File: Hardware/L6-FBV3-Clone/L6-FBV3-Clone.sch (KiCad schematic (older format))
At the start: 25 parts, among them J1 Conn_02x20_Odd_Even, SW1 SW_Push, SW10 SW_Push, SW11 SW_Push, SW12 SW_Push, SW2 SW_Push, SW3 SW_Push, SW4 SW_Push, SW5 SW_Push, SW6 SW_Push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

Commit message: Fixed schematic rule check, assigned components
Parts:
- added J2: PWR, TerminalBlock_Phoenix:TerminalBlock_Phoenix_MPT-0,5-2-2.54_1x02_P2.54mm_Horizontal, symbol Connector:Screw_Terminal_01x02
- D1, D10, D2, D3, D4, D5, D6, D7, D8, D9: footprint (none) -> TerminalBlock_Phoenix:TerminalBlock_Phoenix_MPT-0,5-2-2.54_1x02_P2.54mm_Horizontal
- J1: footprint (none) -> Connector_IDC:IDC-Header_2x20_P2.54mm_Vertical
- R1: footprint (none) -> Resistor_THT:R_Axial_DIN0204_L3.6mm_D1.6mm_P5.08mm_Horizontal
- SW1: value SW_Push -> FX1; footprint (none) -> TerminalBlock_Phoenix:TerminalBlock_Phoenix_MPT-0,5-2-2.54_1x02_P2.54mm_Horizontal
- SW10: value SW_Push -> BNK_UP; footprint (none) -> TerminalBlock_Phoenix:TerminalBlock_Phoenix_MPT-0,5-2-2.54_1x02_P2.54mm_Horizontal
- SW11: value SW_Push -> BNK_DWN; footprint (none) -> TerminalBlock_Phoenix:TerminalBlock_Phoenix_MPT-0,5-2-2.54_1x02_P2.54mm_Horizontal
- SW12: value SW_Push -> ALT; footprint (none) -> TerminalBlock_Phoenix:TerminalBlock_Phoenix_MPT-0,5-2-2.54_1x02_P2.54mm_Horizontal
- SW2: value SW_Push -> FX2; footprint (none) -> TerminalBlock_Phoenix:TerminalBlock_Phoenix_MPT-0,5-2-2.54_1x02_P2.54mm_Horizontal
- SW3: value SW_Push -> FX3; footprint (none) -> TerminalBlock_Phoenix:TerminalBlock_Phoenix_MPT-0,5-2-2.54_1x02_P2.54mm_Horizontal
- SW4: value SW_Push -> FX4; footprint (none) -> TerminalBlock_Phoenix:TerminalBlock_Phoenix_MPT-0,5-2-2.54_1x02_P2.54mm_Horizontal
- SW5: value SW_Push -> FX5; footprint (none) -> TerminalBlock_Phoenix:TerminalBlock_Phoenix_MPT-0,5-2-2.54_1x02_P2.54mm_Horizontal
- SW6: value SW_Push -> PRE_A; footprint (none) -> TerminalBlock_Phoenix:TerminalBlock_Phoenix_MPT-0,5-2-2.54_1x02_P2.54mm_Horizontal
- SW7: value SW_Push -> PRE_B; footprint (none) -> TerminalBlock_Phoenix:TerminalBlock_Phoenix_MPT-0,5-2-2.54_1x02_P2.54mm_Horizontal
- SW8: value SW_Push -> PRE_C; footprint (none) -> TerminalBlock_Phoenix:TerminalBlock_Phoenix_MPT-0,5-2-2.54_1x02_P2.54mm_Horizontal
- SW9: value SW_Push -> PRE_D; footprint (none) -> TerminalBlock_Phoenix:TerminalBlock_Phoenix_MPT-0,5-2-2.54_1x02_P2.54mm_Horizontal
- U1: footprint (none) -> Package_DIP:DIP-24_W7.62mm
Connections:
- net +5V: now also J2.1 (Pin_1)
- net GND: now also J2.2 (Pin_2)
- net PRE_A: now also SW6.1
- no-connect marks 7 -> 29

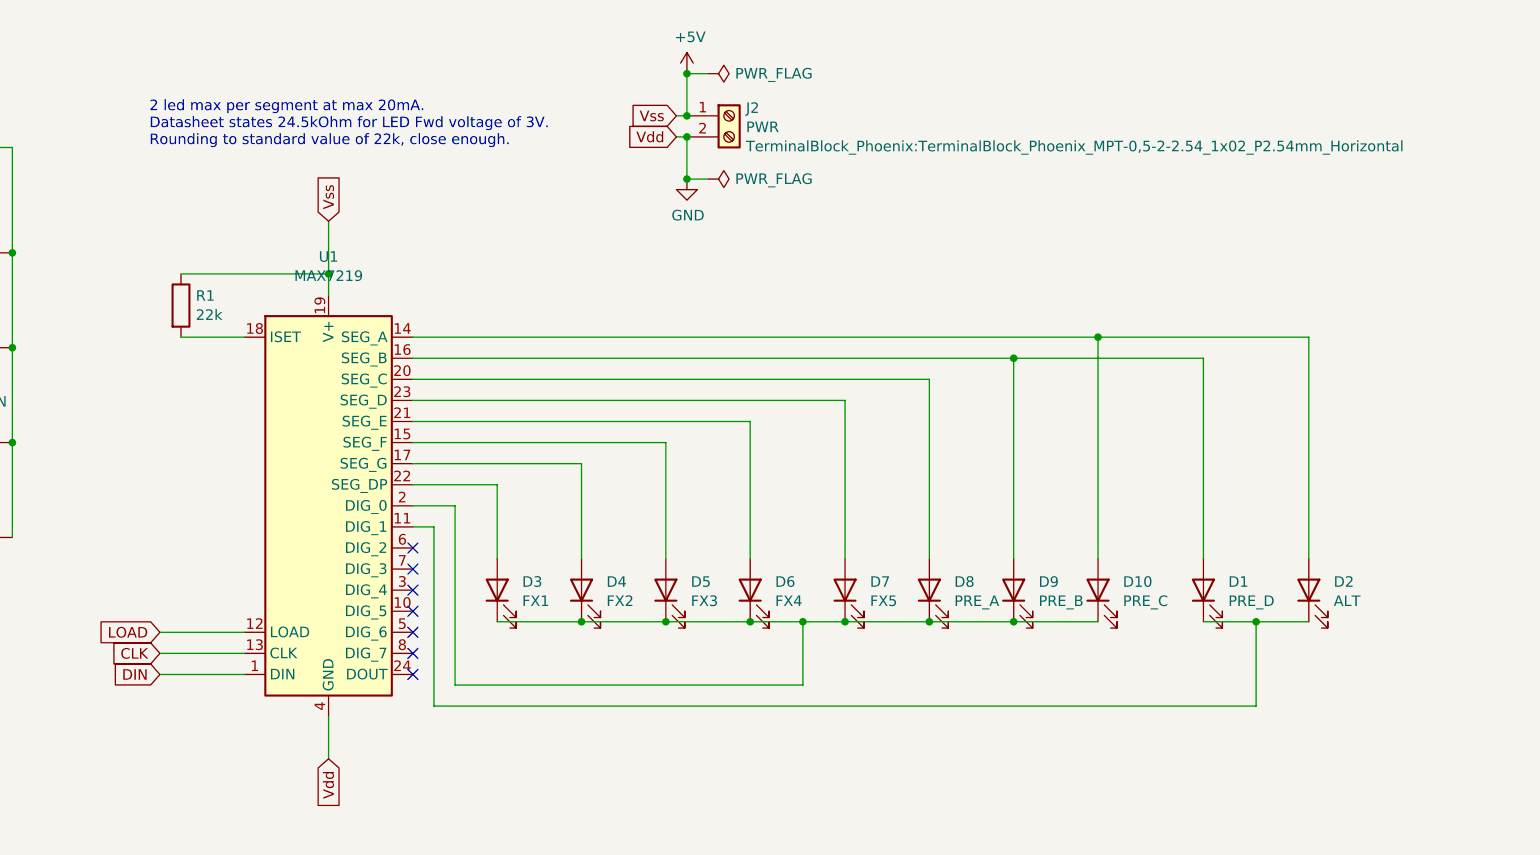
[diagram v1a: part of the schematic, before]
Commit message: Fix to LED assignments
LED HW bug present, needs lower value limiting resistor
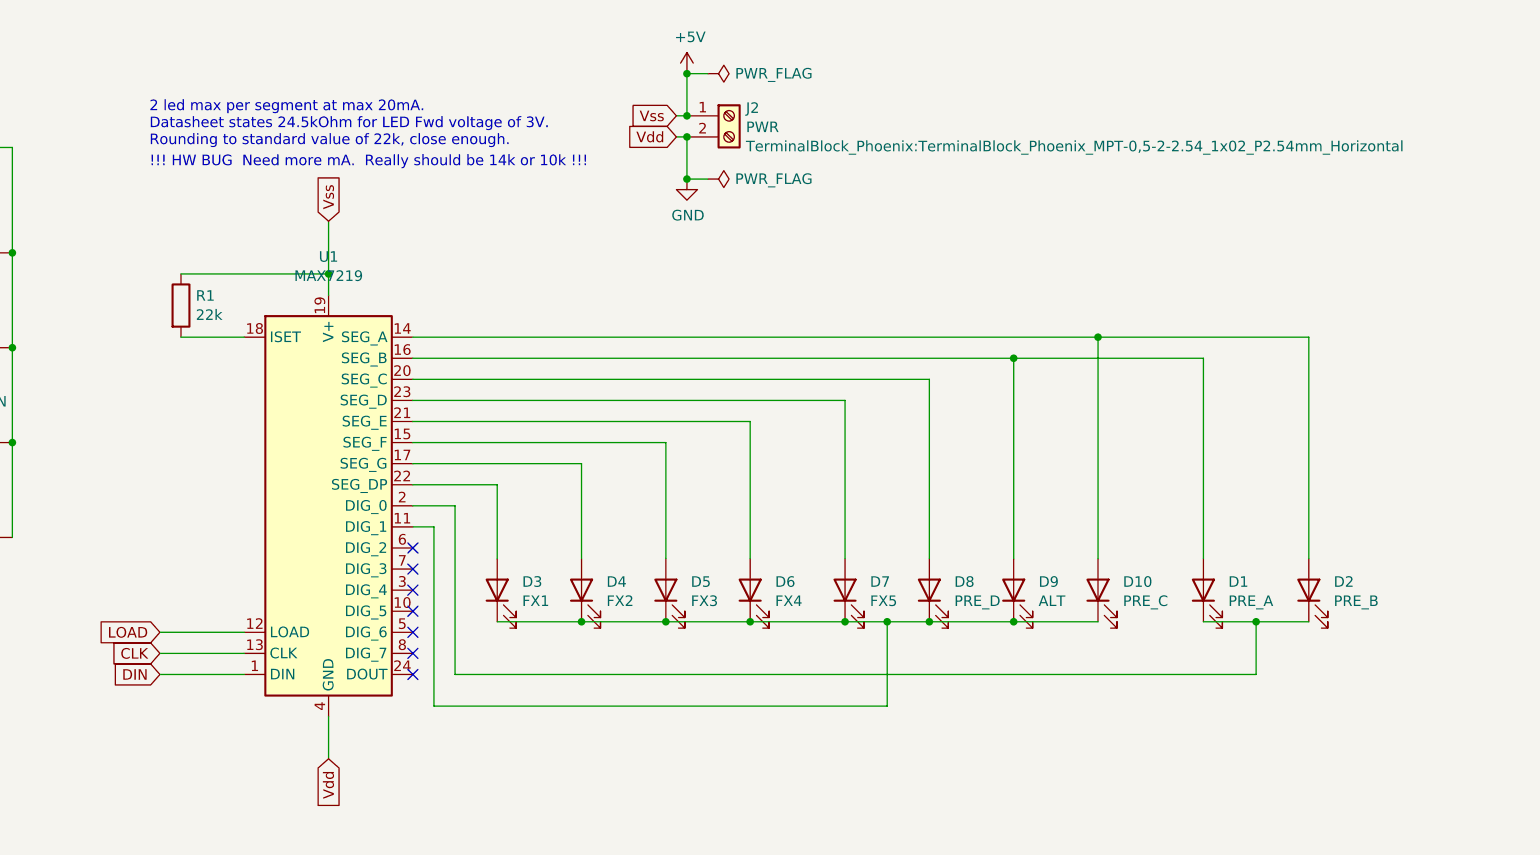
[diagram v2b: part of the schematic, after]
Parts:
- D1: value PRE_D -> PRE_A
- D2: value ALT -> PRE_B
- D8: value PRE_A -> PRE_D
- D9: value PRE_B -> ALT
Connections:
- net at D1.1 (K), D2.1 (K): now also U1.2 (DIG_0); no longer U1.11 (DIG_1)
- net at D10.1 (K), D3.1 (K), D4.1 (K)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: now also U1.11 (DIG_1); no longer U1.2 (DIG_0)
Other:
- note added: "!!! HW BUG Need more mA. Really should be 14k or 10k !!!"
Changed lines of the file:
@@
 P 9000 3250
 F 0 "D9" V 9039 3132 50  0000 R CNN
-F 1 "PRE_B" V 8948 3132 50  0000 R CNN
+F 1 "ALT" V 8948 3132 50  0000 R CNN
 F 2 "TerminalBlock_Phoenix:TerminalBlock_Phoenix_MPT-0,5-2-2.54_1x02_P2.54mm_Horizontal" H 9000 3250 50  0001 C CNN
 F 3 "~" H 9000 3250 50  0001 C CNN
@@
 P 8600 3250
 F 0 "D8" V 8639 3132 50  0000 R CNN
-F 1 "PRE_A" V 8548 3132 50  0000 R CNN
+F 1 "PRE_D" V 8548 3132 50  0000 R CNN
 F 2 "TerminalBlock_Phoenix:TerminalBlock_Phoenix_MPT-0,5-2-2.54_1x02_P2.54mm_Horizontal" H 8600 3250 50  0001 C CNN
 F 3 "~" H 8600 3250 50  0001 C CNN
@@
 P 9900 3250
 F 0 "D1" V 9939 3132 50  0000 R CNN
-F 1 "PRE_D" V 9848 3132 50  0000 R CNN
+F 1 "PRE_A" V 9848 3132 50  0000 R CNN
 F 2 "TerminalBlock_Phoenix:TerminalBlock_Phoenix_MPT-0,5-2-2.54_1x02_P2.54mm_Horizontal" H 9900 3250 50  0001 C CNN
 F 3 "~" H 9900 3250 50  0001 C CNN
@@
 P 10400 3250
 F 0 "D2" V 10439 3132 50  0000 R CNN
-F 1 "ALT" V 10348 3132 50  0000 R CNN
+F 1 "PRE_B" V 10348 3132 50  0000 R CNN
 F 2 "TerminalBlock_Phoenix:TerminalBlock_Phoenix_MPT-0,5-2-2.54_1x02_P2.54mm_Horizontal" H 10400 3250 50  0001 C CNN
 F 3 "~" H 10400 3250 50  0001 C CNN
@@
 	7350 3400 7750 3400
 Connection ~ 7350 3400
-Wire Wire Line
-	7750 3400 8000 3400
 Connection ~ 7750 3400
 Wire Wire Line
-	8200 3400 8600 3400
+	8200 3400 8400 3400
 Connection ~ 8200 3400
 Wire Wire Line
@@
 Connection ~ 9000 3400
 Wire Wire Line
-	9900 3400 10150 3400
-Wire Wire Line
 	6150 2950 6250 2950
 Wire Wire Line
 	6250 2950 6250 3800
 Wire Wire Line
-	6250 3800 10150 3800
-Wire Wire Line
-	10150 3800 10150 3400
-Connection ~ 10150 3400
-Wire Wire Line
-	10150 3400 10400 3400
-Wire Wire Line
 	6150 2850 6350 2850
-Wire Wire Line
-	6350 2850 6350 3700
-Wire Wire Line
-	6350 3700 8000 3700
-Wire Wire Line
-	8000 3700 8000 3400
-Connection ~ 8000 3400
-Wire Wire Line
-	8000 3400 8200 3400
 Wire Wire Line
 	6150 2750 6550 2750
@@
 	7550 1300 7450 1300
 Connection ~ 7450 1300
+Wire Wire Line
+	7750 3400 8200 3400
+Wire Wire Line
+	9900 3400 10150 3400
+Wire Wire Line
+	10150 3400 10150 3650
+Wire Wire Line
+	10150 3650 6350 3650
+Wire Wire Line
+	6350 2850 6350 3650
+Connection ~ 10150 3400
+Wire Wire Line
+	10150 3400 10400 3400
+Wire Wire Line
+	6250 3800 8400 3800
+Wire Wire Line
+	8400 3800 8400 3400
+Connection ~ 8400 3400
+Wire Wire Line
+	8400 3400 8600 3400
+Text Notes 4900 1250 0    50   ~ 0
+!!! HW BUG  Need more mA.  Really should be 14k or 10k !!!
 $EndSCHEMATC
